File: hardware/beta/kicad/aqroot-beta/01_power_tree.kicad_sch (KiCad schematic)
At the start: 53 parts, among them J3 USB_C_Receptacle_USB2.0_16P, J4 JST-PH-2 BATTERY, SW9 SW_SPDT, U10 USBLC6-2SC6, U11 BQ25185, U12 TPS63020, U13 TPS61023, U14 MAX17048

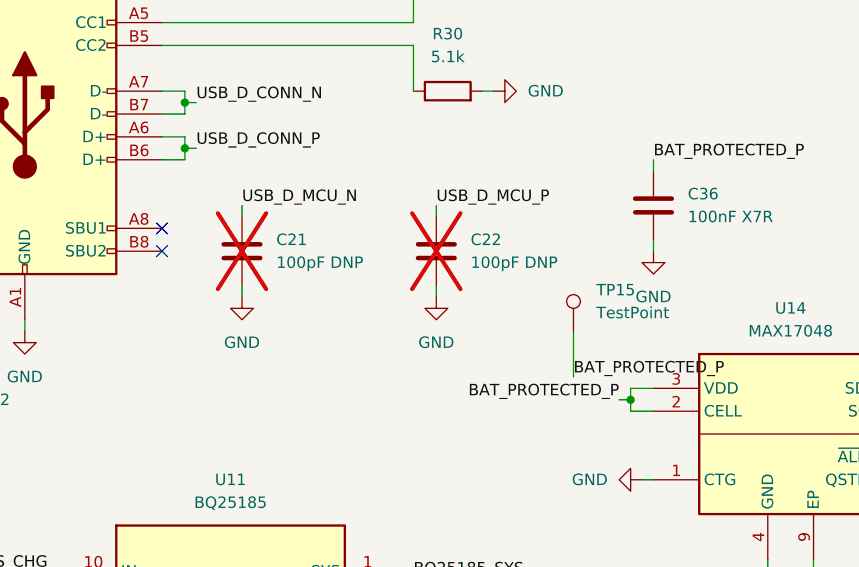
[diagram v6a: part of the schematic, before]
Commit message: set C21 C22 data pins NC for Beta
CTO ruling, Option B locked. C21/C22 stay physically placed at 100 pF DNP
as an optional USB Full-Speed edge-rate / EMI tuning footprint, but their
data-side pins are intentionally NC for Beta. GND pins retained.

Schematic (01_power_tree): deleted the C21 pin-1 stub wire (54.61,57.15)
-> (54.61,58.42) and the C22 pin-1 stub (76.2,57.15) -> (76.2,58.42),
then placed no-connect flags on both data pins. The two local labels
USB_D_MCU_N/P that those stubs terminated into were orphaned by the wire
deletion and removed with them, otherwise ERC gains two new live
label_dangling errors. Hierarchical labels untouched. Added one schematic
note beside the pair.

PCB: net-only sync. C21/C22 pad 1 moved to unconnected-(Cxx-Pad1),
matching the board's existing NC-pin convention. No branch copper existed
or was created. No USB routing in this pass.

ratsnest 440 -> 438 (-2, exactly one per capacitor)
footprints 188, 0 moved; tracks 364; vias 98 - all unchanged
DRC 0 electrical errors, schematic parity 0
ERC 116 / 58 excluded / 58 live - zero new live violations
25 mm USB uncoupled rule and 2.0 mm skew rule unchanged; no DRU change

Co-Authored-By: Claude Opus 5 <noreply@anthropic.com>
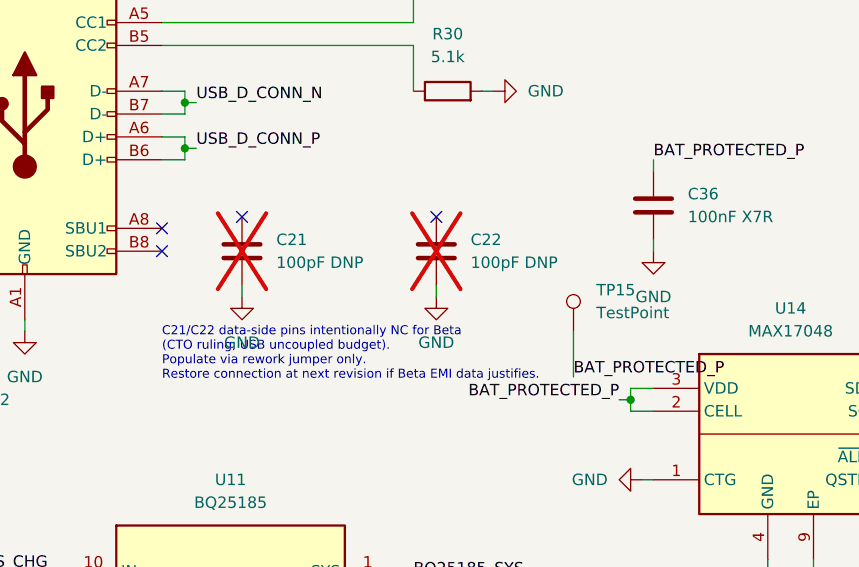
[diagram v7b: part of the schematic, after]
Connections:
- net USB_D_MCU_N: no longer C21.1
- net USB_D_MCU_P: no longer C22.1
- no-connect marks 4 -> 6
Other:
- note added: "C21/C22 data-side pins intentionally NC for Beta (CTO ruling, USB uncoupled budget). Populate via rework jumper only. Restore connection at next revision if Beta EMI data justifies."
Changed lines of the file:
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@@
 	)
 	(no_connect
+		(at 54.61 58.42)
+	)
+	(no_connect
+		(at 76.2 58.42)
+	)
+	(no_connect
 		(at 130.81 87.63)
 	)
@@
 	(wire
 		(pts
-			(xy 54.61 57.15) (xy 54.61 58.42)
-		)
-		(stroke
-			(width 0)
-			(type default)
-		)
-	)
-	(wire
-		(pts
 			(xy 45.72 31.75) (xy 46.99 31.75)
 		)
@@
 	(wire
 		(pts
-			(xy 76.2 57.15) (xy 76.2 58.42)
-		)
-		(stroke
-			(width 0)
-			(type default)
-		)
-	)
-	(wire
-		(pts
 			(xy 190.5 81.28) (xy 190.5 82.55)
 		)
@@
 		)
 	)
-	(label "USB_D_MCU_N"
-		(at 54.61 57.15 0)
-		(effects
-			(font
-				(size 1.27 1.27)
-			)
-			(justify left bottom)
-		)
-	)
-	(label "USB_D_MCU_P"
-		(at 76.2 57.15 0)
-		(effects
-			(font
-				(size 1.27 1.27)
-			)
-			(justify left bottom)
-		)
-	)
 	(label "BQ25185_SYS"
 		(at 133.35 148.59 90)
@@
 		)
 	)
+	(text "C21/C22 data-side pins intentionally NC for Beta\n(CTO ruling, USB uncoupled budget).\nPopulate via rework jumper only.\nRestore connection at next revision if Beta EMI data justifies."
+		(exclude_from_sim no)
+		(at 45.72 73.66 0)
+		(effects
+			(font
+				(size 1 1)
+			)
+			(justify left)
+		)
+	)
